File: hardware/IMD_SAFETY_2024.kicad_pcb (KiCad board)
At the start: 4 copper layers, 66.8 x 60 mm, 97 parts, among them J1 Main- M80-5300842, K2 TE AXICOM IM07DTS, Q1 2N7002, U1 LM393, U10 74HCS08, U13 74HC74, U14 LM393, U15 LM393, U16 LM393, U2 74AC04SC, U3 74LVC1G79, U6 74LVC1G79, U7 MC78M12CDTG, U8 LM1117IMP-5.0, U9 74HCS32

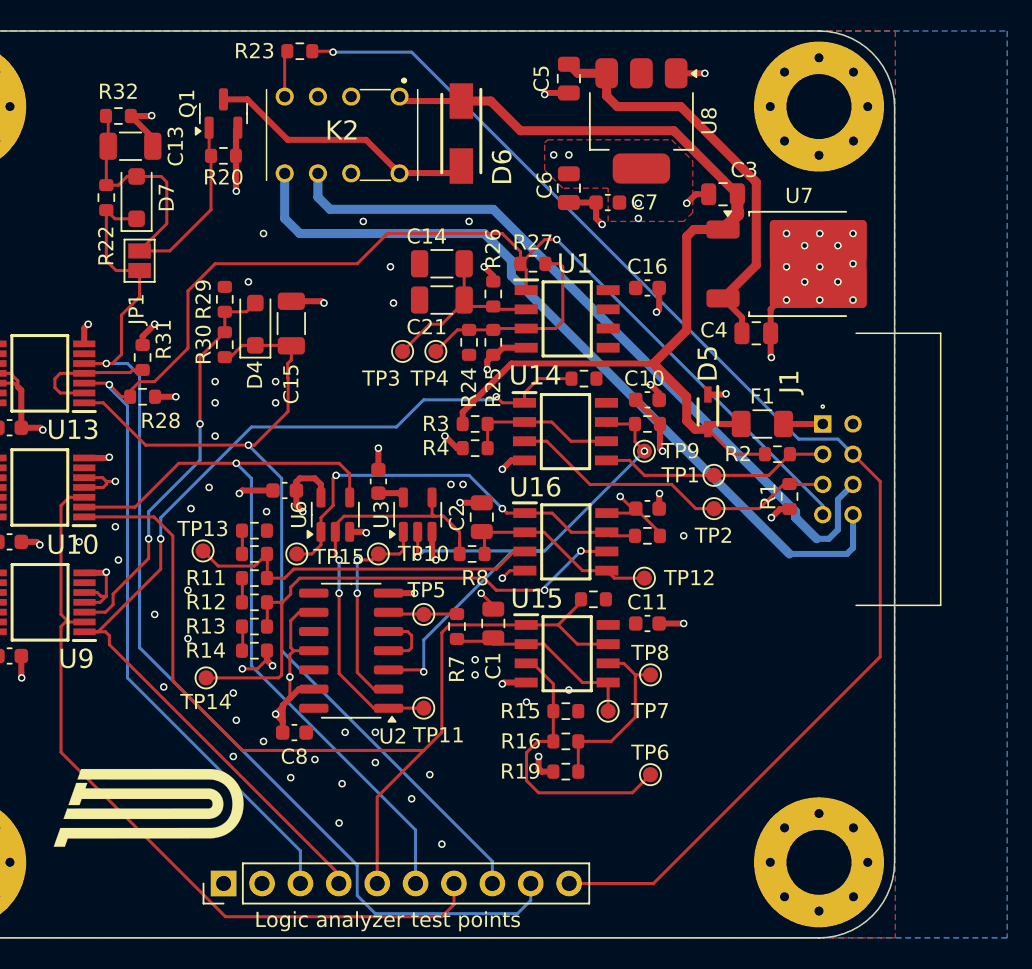
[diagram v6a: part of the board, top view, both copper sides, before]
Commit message: OxDRC state, 2.1.0 ready to review, change connector to vertical, and R-Reset node slightly
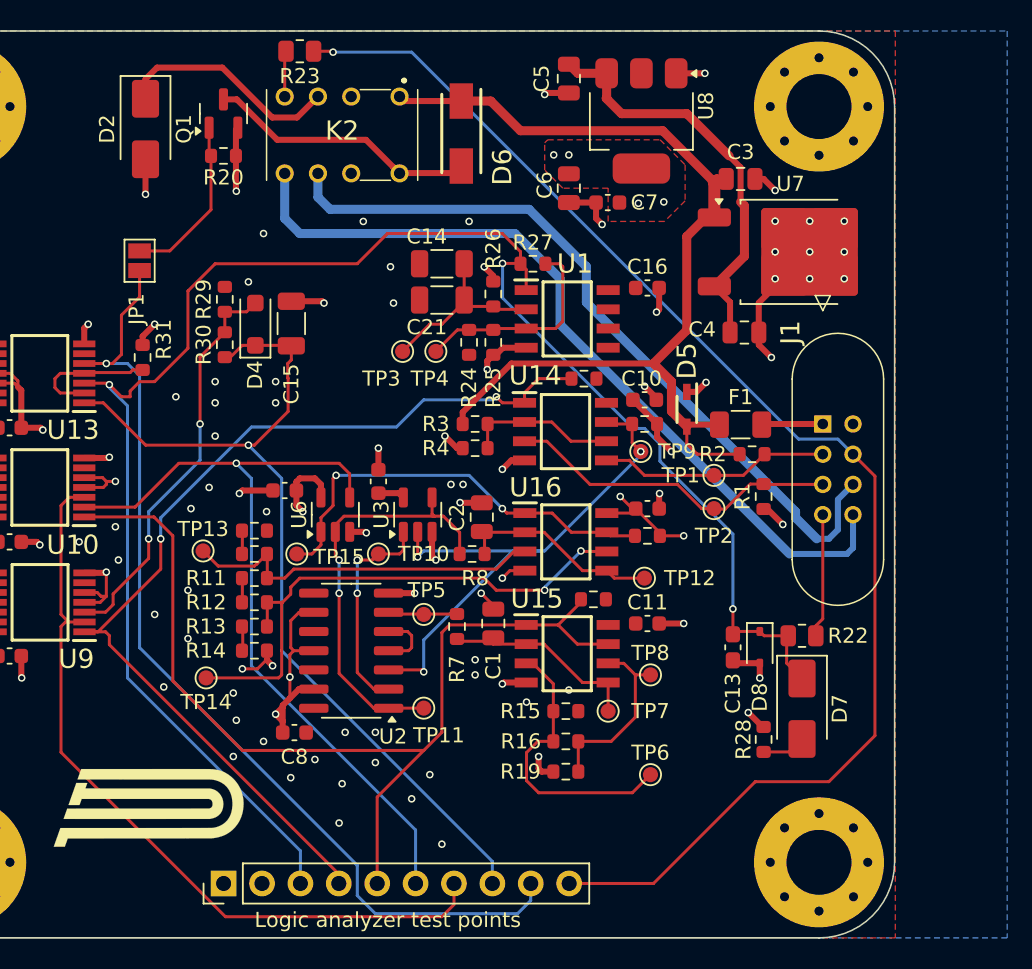
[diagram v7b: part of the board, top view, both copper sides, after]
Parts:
- removed R32: 1M, Resistor_SMD:R_0603_1608Metric
- added D2: SK14, Diode_SMD:D_SMA, F.Cu at (128.2, 67.5)
- added D8: SD05_01FTG, Diode_SMD:D_SOD-323, F.Cu at (168.8, 101.8)
- C13: value 47uF -> 100nF; footprint Capacitor_SMD:C_1206_3216Metric -> Capacitor_SMD:C_0603_1608Metric_Pad1.08x0.95mm_HandSolder
- D7: value SD103BW -> SK14; footprint Diode_SMD:D_SOD-123F -> Diode_SMD:D_SMA
- J1: value Main- M80-5300842 -> Main- M80-5000842; footprint Samacsys:M80-53008YY -> footprints:M80-50008YY_2
- R15: value 400K -> 2.7k
- R16: value 100K -> 5k
- R18: value 2.2K -> 10k
- R19: value 1K -> 100R
- R22: value 100k -> 33R; footprint Resistor_SMD:R_0603_1608Metric -> Resistor_SMD:R_0805_2012Metric
- R23: value 330R -> 33R; footprint Resistor_SMD:R_0603_1608Metric -> Resistor_SMD:R_0805_2012Metric
- R3: value 10K -> 22k
- R4: value 10K -> 3k
- moved D7 55.5 mm to (171.6, 105.8), turned to -90 degrees
- moved R22 54.4 mm to (171.6, 101.0), turned to 0 degrees
- moved C13 51.8 mm to (167.1, 101.8), turned to -90 degrees
- moved R28 46.9 mm to (169.1, 107.9), turned to -90 degrees
- moved R1 1.71 mm to (169.1, 91.8)
- moved R2 1.68 mm to (168.3, 89.0)
- moved C3 1.54 mm to (167.6, 70.8), turned to 0 degrees
- moved F1 1.44 mm to (167.6, 87.0)
- moved D5 1.40 mm to (164.0, 86.0)
- moved U7 0.98 mm to (170.9, 75.6)
- moved C4 0.79 mm to (167.8, 80.9)
- moved TP9 0.24 mm to (161.0, 88.8)
- moved C10 0.19 mm to (161.2, 85.4)
- moved R6 0.19 mm to (161.2, 87.0)
- turned J1 to -90 degrees
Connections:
- C13 pad 1: /NMOS_IN -> RESET
- D7 pad 1: /Q_DFF -> RESET
- D7 pad 2: /NMOS_IN -> Net-(D7-A)
- J1 pad 4: RESET -> EXT_RESET
- K2 pad 3: +5V -> Net-(D2-K)
- R22 pad 1: /NMOS_IN -> RESET
- R22 pad 2: /Q_DFF -> EXT_RESET
- R28 pad 2: RESET -> Net-(D7-A)
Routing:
- net Net-(D2-K): track 0.00 -> 15.0 mm
- net /NMOS_IN: track 25.1 -> 11.2 mm
- net RESET: track 106.1 -> 117.2 mm, vias 2 -> 3
- net EXT_RESET: track 0.00 -> 8.21 mm
- net /Q_DFF: track 73.2 -> 65.1 mm
- net +5V: track 20.2 -> 24.4 mm, vias 48 -> 50
- net Net-(D7-A): track 0.00 -> 2.89 mm
- net +24V: track 67.6 -> 65.0 mm
- net COCKPIT_LED: track 87.8 -> 90.3 mm
- net Net-(J1-Pin_1): track 2.60 -> 4.06 mm
- net SDC_IN: track 49.2 -> 50.6 mm
- net SDC_OUT: track 52.7 -> 53.9 mm
- net GND: track 110.4 -> 111.5 mm, vias 60 -> 56
- net Net-(U3-Q): track 28.6 -> 27.8 mm
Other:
- board text added: "HARDWARE REVISION 2.1.0"
- board text removed: "HARDWARE REVISION 2.0.0"

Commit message: 2.1.0 Release, adjust after review
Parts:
- added C22: 100nF, Capacitor_SMD:C_0603_1608Metric, F.Cu at (156.4, 64.2)
- moved C5 1.85 mm to (154.4, 64.2)
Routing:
- net +12V: track 27.5 -> 29.3 mm
- net GND: track 111.5 -> 113.0 mm
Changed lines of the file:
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@@
 	(footprint "Capacitor_SMD:C_0805_2012Metric"
 		(layer "F.Cu")
-		(at 156.2 64.15 -90)
+		(at 154.354 64.184 -90)
 		(descr "Capacitor SMD 0805 (2012 Metric), square (rectangular) end terminal, IPC_7351 nominal, (Body size source: IPC-SM-782 page 76, https://www.pcb-3d.com/wordpress/wp-content/uploads/ipc-sm-782a_amendment_1_and_2.pdf, https://docs.google.com/spreadsheets/d/1BsfQQcO9C6DZCsRaXUlFlo91Tg2WpOkGARC1WS5S8t0/edit?usp=sharing), generated with kicad-footprint-generator")
 		(tags "capacitor")
@@
 		)
 	)
+	(footprint "Capacitor_SMD:C_0603_1608Metric"
+		(layer "F.Cu")
+		(at 156.386 64.184 -90)
+		(descr "Capacitor SMD 0603 (1608 Metric), square (rectangular) end terminal, IPC_7351 nominal, (Body size source: IPC-SM-782 page 76, https://www.pcb-3d.com/wordpress/wp-content/uploads/ipc-sm-782a_amendment_1_and_2.pdf), generated with kicad-footprint-generator")
+		(tags "capacitor")
+		(property "Reference" "C22"
+			(at 2.286 0.508 180)
+			(layer "F.SilkS")
+			(effects
+				(font
+					(size 1 1)
+					(thickness 0.15)
+				)
+			)
+		)
+		(property "Value" "100nF"
+			(at 0 1.43 90)
+			(layer "F.Fab")
+			(effects
+				(font
+					(size 1 1)
+					(thickness 0.15)
+				)
+			)
+		)
+		(property "Footprint" "Capacitor_SMD:C_0603_1608Metric"
+			(at 0 0 -90)
+			(unlocked yes)
+			(layer "F.Fab")
+			(hide yes)
+			(effects
+				(font
+					(size 1.27 1.27)
+				)
+			)
+		)
+		(property "Datasheet" ""
+			(at 0 0 -90)
+			(unlocked yes)
+			(layer "F.Fab")
+			(hide yes)
+			(effects
+				(font
+					(size 1.27 1.27)
+				)
+			)
+		)
+		(property "Description" "Unpolarized capacitor, small symbol"
+			(at 0 0 -90)
+			(unlocked yes)
+			(layer "F.Fab")
+			(hide yes)
+			(effects
+				(font
+					(size 1.27 1.27)
+				)
+			)
+		)
+		(property ki_fp_filters "C_*")
+		(sheetname "Root")
+		(sheetfile "IMD_SAFETY_2024.kicad_sch")
+		(attr smd)
+		(fp_line
+			(start -0.140581 0.51)
+			(end 0.140581 0.51)
+			(stroke
+				(width 0.12)
+				(type solid)
+			)
+			(layer "F.SilkS")
+		)
+		(fp_line
+			(start -0.140581 -0.51)
+			(end 0.140581 -0.51)
+			(stroke
+				(width 0.12)
+				(type solid)
+			)
+			(layer "F.SilkS")
+		)
+		(fp_line
+			(start -1.48 0.73)
+			(end -1.48 -0.73)
+			(stroke
+				(width 0.05)
+				(type solid)
+			)
+			(layer "F.CrtYd")
+		)
+		(fp_line
+			(start 1.48 0.73)
+			(end -1.48 0.73)
+			(stroke
+				(width 0.05)
+				(type solid)
+			)
+			(layer "F.CrtYd")
+		)
+		(fp_line
+			(start -1.48 -0.73)
+			(end 1.48 -0.73)
+			(stroke
+				(width 0.05)
+				(type solid)
+			)
+			(layer "F.CrtYd")
+		)
+		(fp_line
+			(start 1.48 -0.73)
+			(end 1.48 0.73)
+			(stroke
+				(width 0.05)
+				(type solid)
+			)
+			(layer "F.CrtYd")
+		)
+		(fp_line
+			(start -0.8 0.4)
+			(end -0.8 -0.4)
+			(stroke
+				(width 0.1)
+				(type solid)
+			)
+			(layer "F.Fab")
+		)
+		(fp_line
+			(start 0.8 0.4)
+			(end -0.8 0.4)
+			(stroke
+				(width 0.1)
+				(type solid)
+			)
+			(layer "F.Fab")
+		)
+		(fp_line
+			(start -0.8 -0.4)
+			(end 0.8 -0.4)
+			(stroke
+				(width 0.1)
+				(type solid)
+			)
+			(layer "F.Fab")
+		)
+		(fp_line
+			(start 0.8 -0.4)
+			(end 0.8 0.4)
+			(stroke
+				(width 0.1)
+				(type solid)
+			)
+			(layer "F.Fab")
+		)
+		(fp_text user "${REFERENCE}"
+			(at 0 0 90)
+			(layer "F.Fab")
+			(effects
+				(font
+					(size 0.4 0.4)
+					(thickness 0.06)
+				)
+			)
+		)
+		(pad "1" smd roundrect
+			(at -0.775 0 270)
+			(size 0.9 0.95)
+			(layers "F.Cu" "F.Paste" "F.Mask")
+			(roundrect_rratio 0.25)
+			(net 5 "+12V")
+			(pintype "passive")
+		)
+		(pad "2" smd roundrect
+			(at 0.775 0 270)
+			(size 0.9 0.95)
+			(layers "F.Cu" "F.Paste" "F.Mask")
+			(roundrect_rratio 0.25)
+			(net 2 "GND")
+			(pintype "passive")
+		)
+		(model "${KICAD8_3DMODEL_DIR}/Capacitor_SMD.3dshapes/C_0603_1608Metric.wrl"
+			(offset
+				(xyz 0 0 0)
+			)
+			(scale
+				(xyz 1 1 1)
+			)
+			(rotate
+				(xyz 0 0 0)
+			)
+		)
+	)
 	(footprint "Resistor_SMD:R_0603_1608Metric"
 		(layer "F.Cu")
@@
 			)
 		)
-		(property "Description" ""
+		(property "Description" "Resettable fuse, polymeric positive temperature coefficient"
 			(at 0 0 0)
 			(unlocked yes)
@@
 			)
 		)
-		(property "Mouser#" " 667-ERB-RG0R50V "
+		(property "Mouser#" " 576-1206L050/24WR "
 			(at 0 0 0)
 			(unlocked yes)
@@
 			)
 		)
-		(property ki_fp_filters "*Fuse*")
+		(property ki_fp_filters "*polyfuse* *PTC*")
 		(sheetname "Root")
 		(sheetfile "IMD_SAFETY_2024.kicad_sch")
@@
 			)
 		)
-		(attr exclude_from_pos_files exclude_from_bom)
+		(attr board_only exclude_from_pos_files exclude_from_bom)
 		(fp_circle
 			(center 0 0)
@@
 			)
 		)
-		(attr exclude_from_pos_files exclude_from_bom)
+		(attr board_only exclude_from_pos_files exclude_from_bom)
 		(fp_circle
 			(center 0 0)
@@
 			)
 		)
-		(attr exclude_from_pos_files exclude_from_bom)
+		(attr board_only exclude_from_pos_files exclude_from_bom)
 		(fp_circle
 			(center 0 0)
@@
 			)
 		)
-		(attr exclude_from_pos_files exclude_from_bom)
+		(attr board_only exclude_from_pos_files exclude_from_bom)
 		(fp_circle
 			(center 0 0)
@@
 	)
 	(segment
-		(start 156.2 65.099999)
-		(end 154.700001 65.099999)
-		(width 0.4)
-		(layer "F.Cu")
-		(net 2)
-	)
-	(segment
 		(start 150.8 83.4)
 		(end 150.8 82.825)
@@
 	)
 	(segment
-		(start 154.700001 65.099999)
-		(end 154.6 65.2)
-		(width 0.4)
-		(layer "F.Cu")
-		(net 2)
-	)
-	(segment
 		(start 151.2 77.575)
 		(end 151.2 77.2)
@@
 	)
 	(segment
+		(start 156.386 64.959)
+		(end 154.528999 64.959)
+		(width 0.4)
+		(layer "F.Cu")
+		(net 2)
+	)
+	(segment
 		(start 139.879998 78.879998)
 		(end 140 79)
@@
 	)
 	(segment
+		(start 154.528999 64.959)
+		(end 154.354 65.133999)
+		(width 0.4)
+		(layer "F.Cu")
+		(net 2)
+	)
+	(segment
 		(start 126 90.8)
 		(end 126.2 90.8)
@@
 	)
 	(segment
+		(start 154.354 66.216)
+		(end 154.354 65.133999)
+		(width 0.4)
+		(layer "F.Cu")
+		(net 2)
+	)
+	(segment
 		(start 137.745001 103.745001)
 		(end 137.745001 105.145001)
@@
 	)
 	(via
-		(at 154.6 65.2)
+		(at 154.354 66.216)
 		(size 0.5)
 		(drill 0.3)
@@
 	)
 	(segment
-		(start 159.688 66.47)
-		(end 158.672 65.454)
-		(width 0.6)
-		(layer "F.Cu")
-		(net 5)
-	)
-	(segment
 		(start 158.7 63.8)
-		(end 156.799999 63.8)
+		(end 154.919999 63.8)
 		(width 0.6)
 		(layer "F.Cu")
@@
 	)
 	(segment
-		(start 156.799999 63.8)
-		(end 156.2 63.200001)
+		(start 159.688 66.47)
+		(end 158.672 65.454)
 		(width 0.6)
 		(layer "F.Cu")
@@
 		(width 0.6)
 		(layer "F.Cu")
+		(net 5)
+	)
+	(segment
+		(start 154.919999 63.8)
+		(end 154.354 63.234001)
+		(width 0.6)
+		(layer "F.Cu")
